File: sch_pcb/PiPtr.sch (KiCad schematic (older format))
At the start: 61 parts, among them J101 GLOBAL_LINK_LEFT, J102 GLOBAL_LINK_RIGHT, J107 RASPBERRY_PI, J111 FP_PIXEL, J112 AM2302, Q101 BSS138, Q102 BSS138, Q103 BSS138, Q104 BSS138, Q105 BSS138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

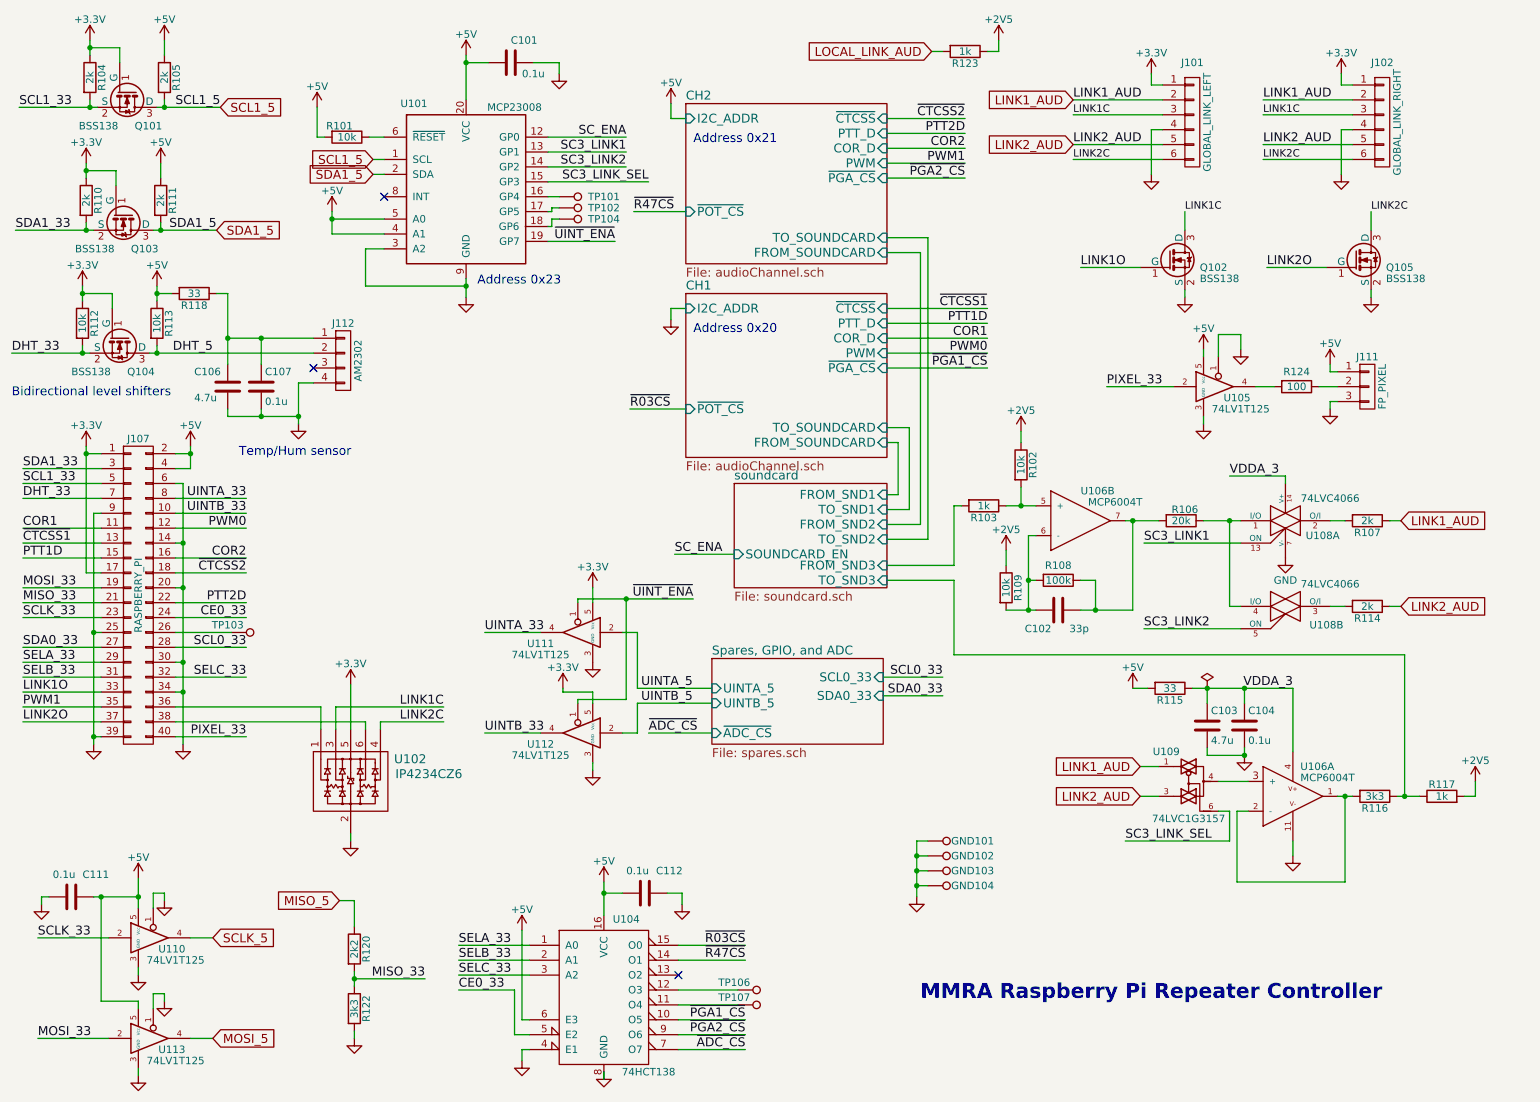
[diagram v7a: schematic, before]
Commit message: Change 33pf to 100pf.  Change 2k and 2200 to 2k2.  Change I2C addresses for MCP23008.  Nudge link connectors
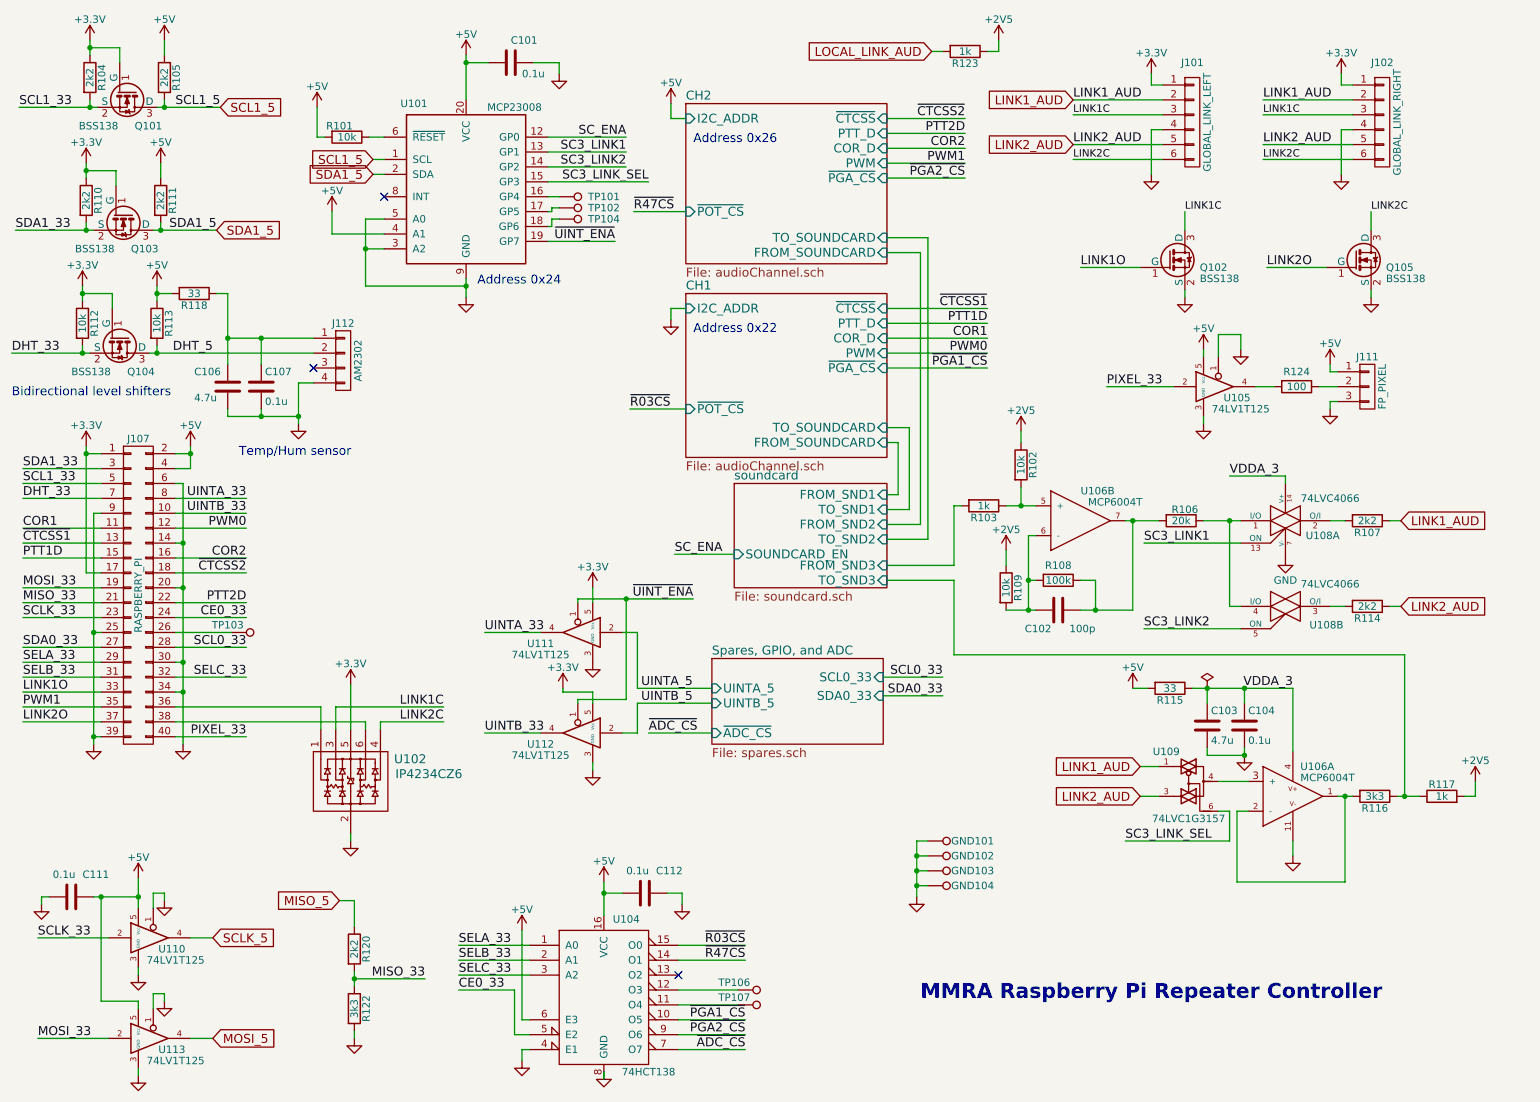
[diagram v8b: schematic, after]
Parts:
- C102: value 33p -> 100p
- Q101: Digikey PN (none) -> 7-1142-1-ND
- R104, R105, R107, R110, R111, R114: value 2k -> 2k2
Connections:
- net +5V: no longer U101.5 (A0)
- net GND: now also U101.5 (A0)
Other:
- note added: "Address 0x22"
- note added: "Address 0x24"
- note added: "Address 0x26"
- note removed: "Address 0x20"
- note removed: "Address 0x21"
- note removed: "Address 0x23"
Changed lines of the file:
@@
 F 2 "lib:SOT23" H 1500 975 50  0001 L CIN
 F 3 "" H 1300 1050 50  0001 L CNN
+F 4 "7-1142-1-ND" V 1300 1050 60  0001 C CNN "Digikey PN"
 	1    1300 1050
 	0    1    1    0
@@
 P 1050 950
 F 0 "R104" V 1130 950 50  0000 C CNN
-F 1 "2k" V 1050 950 50  0000 C CNN
+F 1 "2k2" V 1050 950 50  0000 C CNN
 F 2 "lib:smd0603" V 980 950 50  0001 C CNN
 F 3 "" H 1050 950 50  0001 C CNN
@@
 P 1550 950
 F 0 "R105" V 1630 950 50  0000 C CNN
-F 1 "2k" V 1550 950 50  0000 C CNN
+F 1 "2k2" V 1550 950 50  0000 C CNN
 F 2 "lib:smd0603" V 1480 950 50  0001 C CNN
 F 3 "" H 1550 950 50  0001 C CNN
@@
 P 1025 1775
 F 0 "R110" V 1105 1775 50  0000 C CNN
-F 1 "2k" V 1025 1775 50  0000 C CNN
+F 1 "2k2" V 1025 1775 50  0000 C CNN
 F 2 "lib:smd0603" V 955 1775 50  0001 C CNN
 F 3 "" H 1025 1775 50  0001 C CNN
@@
 P 1525 1775
 F 0 "R111" V 1605 1775 50  0000 C CNN
-F 1 "2k" V 1525 1775 50  0000 C CNN
+F 1 "2k2" V 1525 1775 50  0000 C CNN
 F 2 "lib:smd0603" V 1455 1775 50  0001 C CNN
 F 3 "" H 1525 1775 50  0001 C CNN
@@
 $EndComp
 Text Notes 5100 1400 0    60   ~ 0
-Address 0x21
+Address 0x26
 Text Label 7875 3025 0    60   ~ 0
 PIXEL_33
@@
 P 7550 4525
 F 0 "C102" V 7675 4300 50  0000 L CNN
-F 1 "33p" V 7675 4600 50  0000 L CNN
+F 1 "100p" V 7675 4600 50  0000 L CNN
 F 2 "lib:smd0603" H 7588 4375 50  0001 C CNN
 F 3 "" H 7550 4525 50  0001 C CNN
@@
 P 9625 3925
 F 0 "R107" V 9705 3925 50  0000 C CNN
-F 1 "2k" V 9625 3925 50  0000 C CNN
+F 1 "2k2" V 9625 3925 50  0000 C CNN
 F 2 "lib:smd0603" V 9555 3925 50  0001 C CNN
 F 3 "" H 9625 3925 50  0001 C CNN
@@
 P 9625 4500
 F 0 "R114" V 9705 4500 50  0000 C CNN
-F 1 "2k" V 9625 4500 50  0000 C CNN
+F 1 "2k2" V 9625 4500 50  0000 C CNN
 F 2 "lib:smd0603" V 9555 4500 50  0001 C CNN
 F 3 "" H 9625 4500 50  0001 C CNN
@@
 SDA1_5
 Text Notes 5100 2675 0    60   ~ 0
-Address 0x20
+Address 0x22
 Wire Wire Line
 	4950 1125 4950 1225
@@
 	2950 1500 3025 1500
 Wire Wire Line
-	2900 2100 2900 2350
+	2900 1900 2900 2350
 Wire Wire Line
 	2900 2350 3575 2350
@@
 	3025 2100 2900 2100
 Wire Wire Line
-	3025 1900 2675 1900
-Wire Wire Line
-	2675 1850 2675 2000
-Wire Wire Line
 	2675 2000 3025 2000
-Connection ~ 2675 1900
 $Comp
 L +5V #PWR0131
@@
 $EndComp
 Text Notes 3650 2350 0    60   ~ 0
-Address 0x23
+Address 0x24
 Wire Wire Line
 	8775 4075 8125 4075
@@
 	1    0    0    -1
 $EndComp
+Wire Wire Line
+	2675 1850 2675 2000
+Wire Wire Line
+	2900 1900 3025 1900
+Connection ~ 2900 2100
 $EndSCHEMATC
